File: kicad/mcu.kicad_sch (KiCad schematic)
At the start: 32 parts, among them SW1 BOOT, U3 STM32F405RGT6, Y1 8MHz

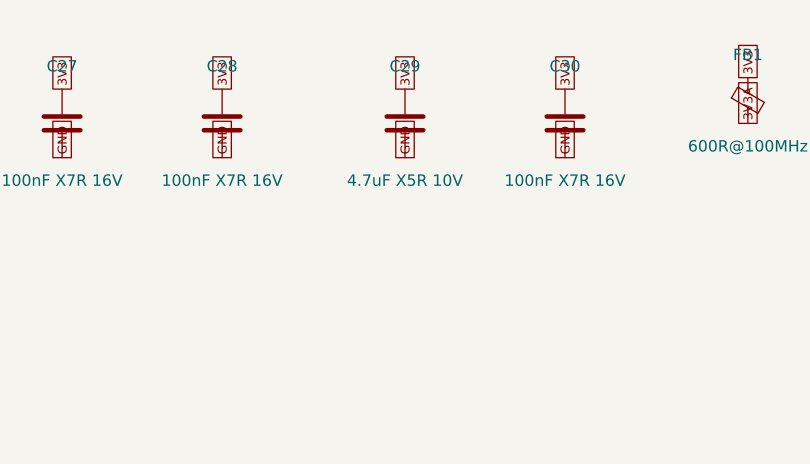
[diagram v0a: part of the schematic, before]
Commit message: Gate 1 fixes (crystal gm evidence, LDO output ESR, X7R caps, 50V HF cap, per-MPN datasheets, in_bom flags, project-file merge, parity fields), power re-audit fixes (board-level thermal envelope, USB inrush deviation, R41 VTX 0R link), PCB placement + legalizer + grommet keepouts; Gate 1 reports
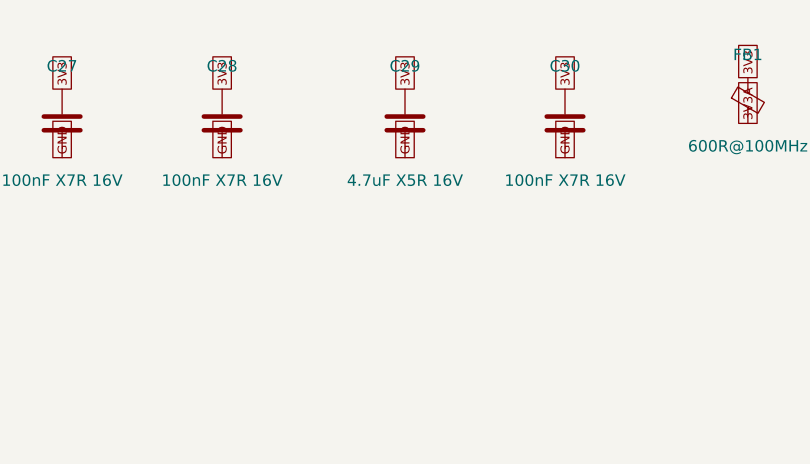
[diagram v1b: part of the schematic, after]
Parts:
- C29: value 4.7uF X5R 10V -> 4.7uF X5R 16V
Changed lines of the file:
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@@
 			)
 		)
-		(property "Datasheet" "https://product.samsungsem.com/mlcc/"
+		(property "Datasheet" "https://product.samsungsem.com/mlcc/CL05B104KO5NNNC.do"
 			(at 109.22 35.56 0)
 			(effects
@@
 			)
 		)
-		(property "Datasheet" "https://product.samsungsem.com/mlcc/"
+		(property "Datasheet" "https://product.samsungsem.com/mlcc/CL05B104KO5NNNC.do"
 			(at 127 35.56 0)
 			(effects
@@
 			)
 		)
-		(property "Datasheet" "https://product.samsungsem.com/mlcc/"
+		(property "Datasheet" "https://product.samsungsem.com/mlcc/CL05B104KO5NNNC.do"
 			(at 147.32 35.56 0)
 			(effects
@@
 			)
 		)
-		(property "Datasheet" "https://product.samsungsem.com/mlcc/"
+		(property "Datasheet" "https://product.samsungsem.com/mlcc/CL05B104KO5NNNC.do"
 			(at 165.1 35.56 0)
 			(effects
@@
 			)
 		)
-		(property "Value" "4.7uF X5R 10V"
+		(property "Value" "4.7uF X5R 16V"
 			(at 185.42 41.91 0)
 			(effects
@@
 			)
 		)
-		(property "Datasheet" "https://product.samsungsem.com/mlcc/"
+		(property "Datasheet" "https://product.samsungsem.com/mlcc/CL10A475KO8NNNC.do"
 			(at 185.42 35.56 0)
 			(effects
@@
 			)
 		)
-		(property "Datasheet" "https://product.samsungsem.com/mlcc/"
+		(property "Datasheet" "https://product.samsungsem.com/mlcc/CL05B104KO5NNNC.do"
 			(at 203.2 35.56 0)
 			(effects
@@
 			)
 		)
-		(property "Datasheet" "https://product.samsungsem.com/mlcc/"
+		(property "Datasheet" "https://product.samsungsem.com/mlcc/CL10A105KA8NNNC.do"
 			(at 243.84 35.56 0)
 			(effects
@@
 			)
 		)
-		(property "Datasheet" "https://product.samsungsem.com/mlcc/"
+		(property "Datasheet" "https://product.samsungsem.com/mlcc/CL05B104KO5NNNC.do"
 			(at 266.7 35.56 0)
 			(effects
@@
 			)
 		)
-		(property "Datasheet" "https://product.samsungsem.com/mlcc/"
+		(property "Datasheet" "https://product.samsungsem.com/mlcc/CL10A225KO8NNNC.do"
 			(at 287.02 35.56 0)
 			(effects
@@
 			)
 		)
-		(property "Datasheet" "https://product.samsungsem.com/mlcc/"
+		(property "Datasheet" "https://product.samsungsem.com/mlcc/CL10A225KO8NNNC.do"
 			(at 309.88 35.56 0)
 			(effects
@@
 			)
 		)
-		(property "Datasheet" "https://product.samsungsem.com/mlcc/"
+		(property "Datasheet" "https://product.samsungsem.com/mlcc/CL05B104KO5NNNC.do"
 			(at 332.74 35.56 0)
 			(effects
@@
 			)
 		)
-		(property "Datasheet" "https://product.samsungsem.com/mlcc/"
+		(property "Datasheet" "https://product.samsungsem.com/mlcc/CL05C100JB5NNNC.do"
 			(at 83.82 149.86 0)
 			(effects
@@
 			)
 		)
-		(property "Datasheet" "https://product.samsungsem.com/mlcc/"
+		(property "Datasheet" "https://product.samsungsem.com/mlcc/CL05C100JB5NNNC.do"
 			(at 111.76 149.86 0)
 			(effects

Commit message: Gate 0 complete (power re-audit round 3 PASS); Gate 1 MCU crystal fix (8.2 pF loads, ECX-32 C0 evidence); net classes; staged board build; routing pipeline; placement renders; raw BOM
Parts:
- C36, C37: value 10pF C0G 50V -> 8.2pF C0G 50V; DigiKey 1276-1621-1-ND (verify) -> 1276-1650-1-ND (verify); MPN CL05C100JB5NNNC -> CL05C8R2CB5NNNC
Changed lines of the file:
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@@
 			)
 		)
-		(property "Value" "10pF C0G 50V"
+		(property "Value" "8.2pF C0G 50V"
 			(at 83.82 156.21 0)
 			(effects
@@
 			)
 		)
-		(property "Datasheet" "https://product.samsungsem.com/mlcc/CL05C100JB5NNNC.do"
+		(property "Datasheet" "https://product.samsungsem.com/mlcc/CL05C8R2CB5NNNC.do"
 			(at 83.82 149.86 0)
 			(effects
@@
 			)
 		)
-		(property "MPN" "CL05C100JB5NNNC"
+		(property "MPN" "CL05C8R2CB5NNNC"
 			(at 83.82 149.86 0)
 			(effects
@@
 			)
 		)
-		(property "DigiKey" "1276-1621-1-ND (verify)"
+		(property "DigiKey" "1276-1650-1-ND (verify)"
 			(at 83.82 149.86 0)
 			(effects
@@
 			)
 		)
-		(property "Value" "10pF C0G 50V"
+		(property "Value" "8.2pF C0G 50V"
 			(at 111.76 156.21 0)
 			(effects
@@
 			)
 		)
-		(property "Datasheet" "https://product.samsungsem.com/mlcc/CL05C100JB5NNNC.do"
+		(property "Datasheet" "https://product.samsungsem.com/mlcc/CL05C8R2CB5NNNC.do"
 			(at 111.76 149.86 0)
 			(effects
@@
 			)
 		)
-		(property "MPN" "CL05C100JB5NNNC"
+		(property "MPN" "CL05C8R2CB5NNNC"
 			(at 111.76 149.86 0)
 			(effects
@@
 			)
 		)
-		(property "DigiKey" "1276-1621-1-ND (verify)"
+		(property "DigiKey" "1276-1650-1-ND (verify)"
 			(at 111.76 149.86 0)
 			(effects

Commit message: Gate 2 sourcing: apply DigiKey drop-in replacements (G2S-01/02/03/09), PN corrections, regenerate BOM; sourcing report and DigiKey BOM CSVs
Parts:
- C29: DigiKey 1276-1044-1-ND (verify) -> 1276-1784-1-ND
- C33, C34: DigiKey 1276-1183-1-ND (verify) -> 1276-1040-1-ND
- C36, C37: DigiKey 1276-1650-1-ND (verify) -> 399-C0402C829C5GACTUCT-ND; MPN CL05C8R2CB5NNNC -> C0402C829C5GACTU; Manufacturer Samsung Electro-Mechanics -> KEMET
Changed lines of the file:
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@@
 			)
 		)
-		(property "DigiKey" "1276-1044-1-ND (verify)"
+		(property "DigiKey" "1276-1784-1-ND"
 			(at 185.42 35.56 0)
 			(effects
@@
 			)
 		)
-		(property "DigiKey" "1276-1183-1-ND (verify)"
+		(property "DigiKey" "1276-1040-1-ND"
 			(at 287.02 35.56 0)
 			(effects
@@
 			)
 		)
-		(property "DigiKey" "1276-1183-1-ND (verify)"
+		(property "DigiKey" "1276-1040-1-ND"
 			(at 309.88 35.56 0)
 			(effects
@@
 			)
 		)
-		(property "Datasheet" "https://product.samsungsem.com/mlcc/CL05C8R2CB5NNNC.do"
+		(property "Datasheet" "https://content.kemet.com/datasheets/KEM_C1003_C0G_SMD.pdf"
 			(at 83.82 149.86 0)
 			(effects
@@
 			)
 		)
-		(property "MPN" "CL05C8R2CB5NNNC"
+		(property "MPN" "C0402C829C5GACTU"
 			(at 83.82 149.86 0)
 			(effects
@@
 			)
 		)
-		(property "Manufacturer" "Samsung Electro-Mechanics"
+		(property "Manufacturer" "KEMET"
 			(at 83.82 149.86 0)
 			(effects
@@
 			)
 		)
-		(property "DigiKey" "1276-1650-1-ND (verify)"
+		(property "DigiKey" "399-C0402C829C5GACTUCT-ND"
 			(at 83.82 149.86 0)
 			(effects
@@
 			)
 		)
-		(property "Datasheet" "https://product.samsungsem.com/mlcc/CL05C8R2CB5NNNC.do"
+		(property "Datasheet" "https://content.kemet.com/datasheets/KEM_C1003_C0G_SMD.pdf"
 			(at 111.76 149.86 0)
 			(effects
@@
 			)
 		)
-		(property "MPN" "CL05C8R2CB5NNNC"
+		(property "MPN" "C0402C829C5GACTU"
 			(at 111.76 149.86 0)
 			(effects
@@
 			)
 		)
-		(property "Manufacturer" "Samsung Electro-Mechanics"
+		(property "Manufacturer" "KEMET"
 			(at 111.76 149.86 0)
 			(effects
@@
 			)
 		)
-		(property "DigiKey" "1276-1650-1-ND (verify)"
+		(property "DigiKey" "399-C0402C829C5GACTUCT-ND"
 			(at 111.76 149.86 0)
 			(effects

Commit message: D-24: unused-pin pulldowns R21-R24 removed (routing space under the MCU); schematic regenerated (ERC 0, netcheck OK), BOM 119 placements, est. $173.28
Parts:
- removed R21, R22, R23, R24: 100K, Resistor_SMD:R_0402_1005Metric, symbol Device:R
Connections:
- net UNUSED_PB12: no longer names the net of U3.33 (PB12)
- net UNUSED_PB13: no longer names the net of U3.34 (PB13)
- net UNUSED_PC2: no longer names the net of U3.10 (PC2)
- net UNUSED_PC3: no longer names the net of U3.11 (PC3)
- no-connect marks 0 -> 4
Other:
- moved on the sheet: D11, D12, R25, R26, R27, R28

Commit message: Readable schematic: functional blocks with titles, passives wired to their IC pins, GND power symbols, per-rail decoupling banks, labels only between blocks (ERC 0, netcheck OK, same nets)
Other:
- note added: "3V3 decoupling / bulk"
- note added: "3V3A decoupling / bulk"
- note added: "U3 STM32F405RGT6 - MCU 168 MHz Cortex-M4F, LQFP-64"
- note added: "Y1 8MHz - 8 MHz HSE crystal, CL 8 pF"
- moved on the sheet: C25, C26, C27, C28, C29, C30, C31, C32, C33, C34, C35, C36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

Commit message: Rev D: Gate 4 MAJOR re-route, Gate 6 front mark, smoke red-team guide fixes; outputs regenerated
- G4D-02: router-only AVOID boxes keep foreign nets off B.Cu inside the U1/U2 buck footprints; SPI1_MOSI, LED_DIN, MOTOR8
  re-routed out of them
- G4D-01: CURR_ADC re-routed 70.4 mm / 3 vias -> 16.7 mm / 2 vias
- G6B-01: board front marked by silk arrows (FRONT at the J3 edge on the bottom, FWD on the top); G6B-03: P6/J5 labels placed
  (0.8 mm, footprint silk now an obstacle), docs/config name the marks
- G6S-11: LDOs first powered at 3.6 V / 30 mA on 5V_SYS before 8.4 V; G6S-12 rail-to-rail checks; G6S-14 ESC harness check
- G6S-19: power.md (VBAT zone on In3, BAT54S removed, rev D), schematic title block rev D
DRC: 0 errors, 0 unconnected, 0 parity; warnings: 16 dangling vias, 1 silk overlap (C44/U8). placecheck PASS.
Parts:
- Y1: DigiKey 50-ECS-80-8-33-JEN-TR3CT-ND (verify) -> 50-ECS-80-8-33-JEN-TR3CT-ND
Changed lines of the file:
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@@
 	(title_block
 		(title "F405-FC flight controller - MCU")
-		(rev "C")
+		(rev "D")
 		(company "F405-FC")
 	)
@@
 			)
 		)
-		(property "DigiKey" "50-ECS-80-8-33-JEN-TR3CT-ND (verify)"
+		(property "DigiKey" "50-ECS-80-8-33-JEN-TR3CT-ND"
 			(at 261.62 30.48 0)
 			(effects
